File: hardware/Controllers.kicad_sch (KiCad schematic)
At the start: 1 part

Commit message: NEW SCHEMATIC
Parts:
- removed D7: D_TVS, symbol Device:D_TVS
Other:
- removed sheet IC_4
- added sheet IC_0 (ic_0.kicad_sch)
- sheet IC_1: file IC.kicad_sch -> ic_1.kicad_sch
- sheet IC_1 ports: added FUSE_IS1, LHI1, NSS, OUT1_0, OUT1_1, OUT1_2, OUT1_3, SCK; removed CSN, IS, LHI, OUT0, OUT1, OUT2, OUT3, SCLK
- sheet IC_2: file IC.kicad_sch -> ic_2.kicad_sch
- sheet IC_2 ports: added FUSE_IS2, LHI2, NSS, OUT2_0, OUT2_1, OUT2_2, OUT2_3, SCK; removed CSN, IS, LHI, OUT0, OUT1, OUT2, OUT3, SCLK
- sheet IC_3: file IC.kicad_sch -> ic_3.kicad_sch
- sheet IC_3 ports: added FUSE_IS3, LHI3, NSS, OUT3_0, OUT3_1, OUT3_2, OUT3_3, SCK; removed CSN, IS, LHI, OUT0, OUT1, OUT2, OUT3, SCLK
- note removed: "clk"
- note removed: "nss"
- note removed: "tvs na schemacie z konektorem"
- company: (none) -> Authors: Grzegorz Potocki Jędrzej Kasprzyk
- title: (none) -> PDUv3

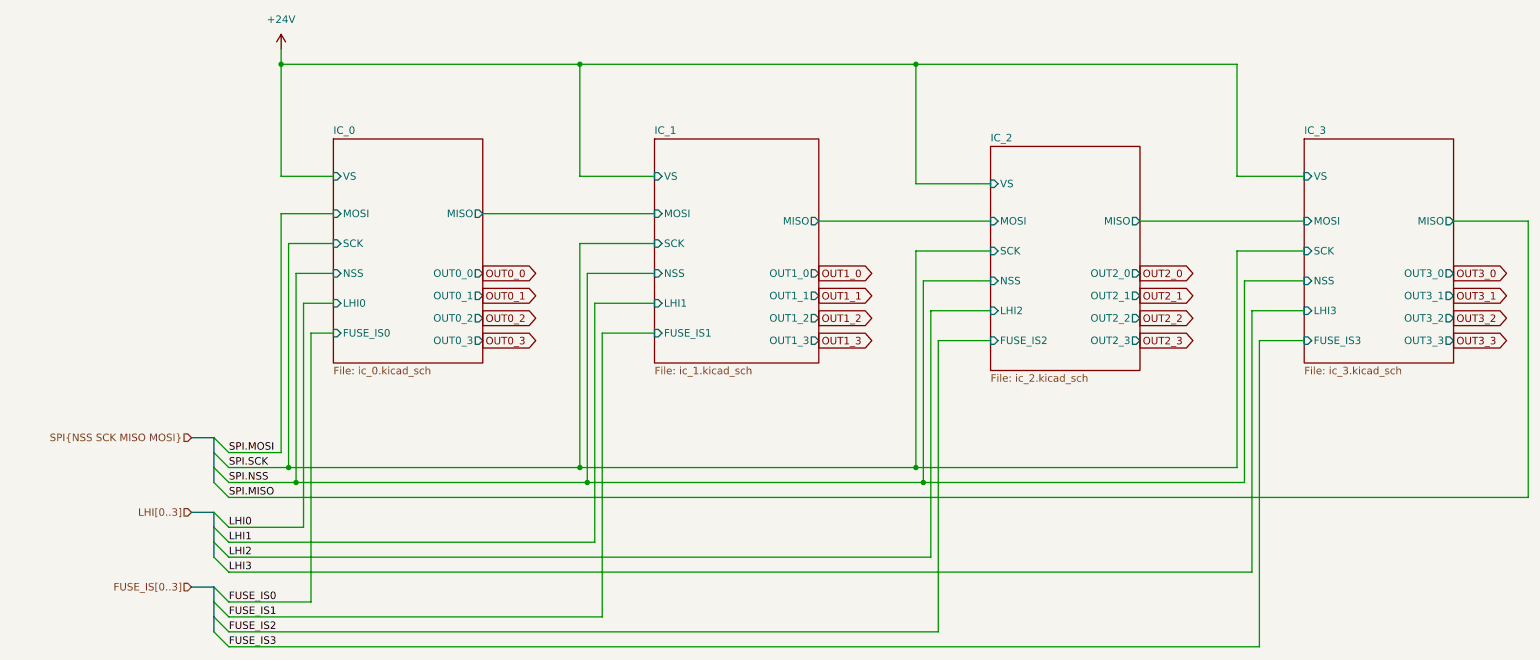
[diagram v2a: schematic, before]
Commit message: new pcb layout & can coppied from steeringwheel
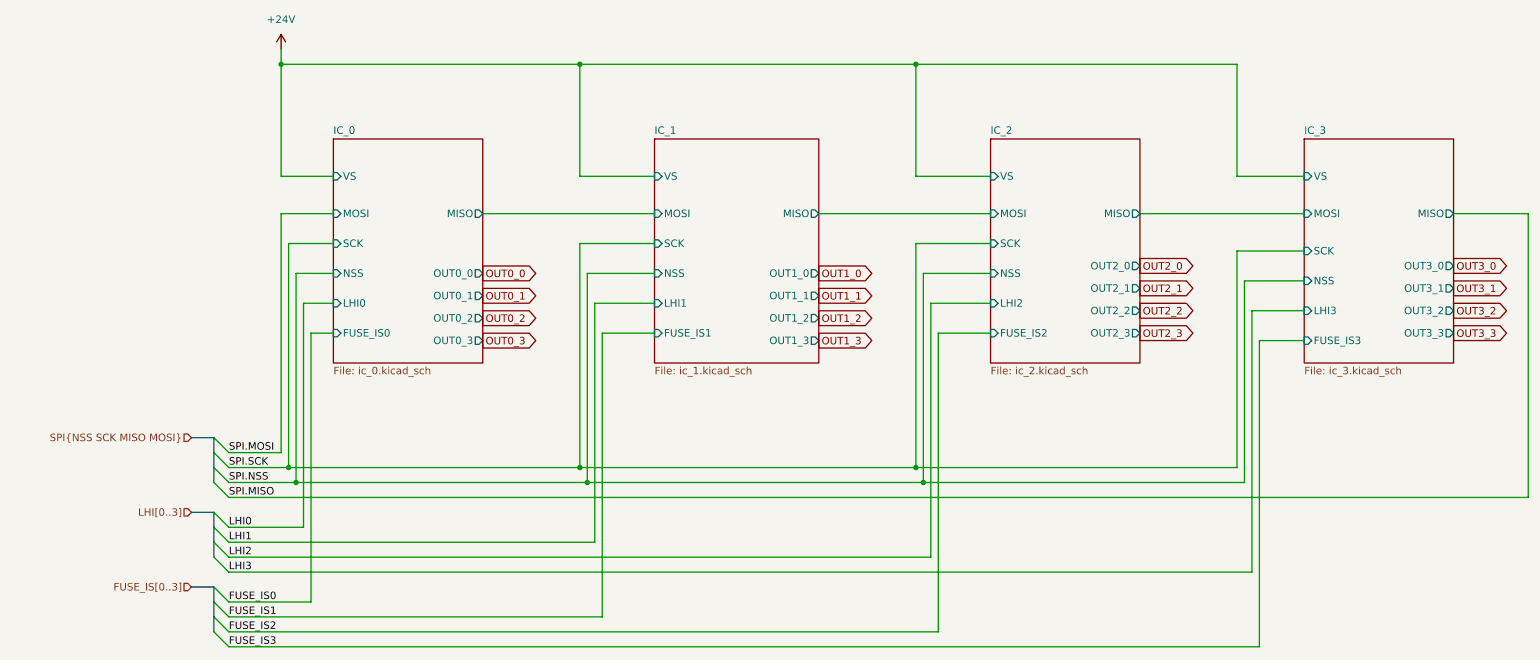
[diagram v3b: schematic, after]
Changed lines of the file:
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@@
 	(wire
 		(pts
-			(xy 171.45 134.62) (xy 171.45 92.71)
+			(xy 171.45 134.62) (xy 171.45 91.44)
 		)
 		(stroke
@@
 	(wire
 		(pts
-			(xy 170.18 87.63) (xy 181.61 87.63)
+			(xy 170.18 86.36) (xy 181.61 86.36)
 		)
 		(stroke
@@
 	(wire
 		(pts
-			(xy 273.05 77.47) (xy 260.35 77.47)
+			(xy 273.05 76.2) (xy 260.35 76.2)
 		)
 		(stroke
@@
 	(wire
 		(pts
-			(xy 181.61 97.79) (xy 172.72 97.79)
-		)
-		(stroke
-			(width 0)
-			(type default)
-		)
-	)
-	(wire
-		(pts
-			(xy 207.01 77.47) (xy 234.95 77.47)
+			(xy 181.61 96.52) (xy 172.72 96.52)
+		)
+		(stroke
+			(width 0)
+			(type default)
+		)
+	)
+	(wire
+		(pts
+			(xy 207.01 76.2) (xy 234.95 76.2)
 		)
 		(stroke
@@
 	(wire
 		(pts
-			(xy 273.05 124.46) (xy 273.05 77.47)
+			(xy 273.05 124.46) (xy 273.05 76.2)
 		)
 		(stroke
@@
 	(wire
 		(pts
-			(xy 168.91 71.12) (xy 181.61 71.12)
+			(xy 168.91 69.85) (xy 181.61 69.85)
 		)
 		(stroke
@@
 	(wire
 		(pts
+			(xy 152.4 76.2) (xy 181.61 76.2)
+		)
+		(stroke
+			(width 0)
+			(type default)
+		)
+	)
+	(wire
+		(pts
 			(xy 111.76 119.38) (xy 111.76 81.28)
 		)
@@
 	(wire
 		(pts
-			(xy 170.18 121.92) (xy 170.18 87.63)
+			(xy 170.18 121.92) (xy 170.18 86.36)
 		)
 		(stroke
@@
 	(wire
 		(pts
-			(xy 171.45 92.71) (xy 181.61 92.71)
-		)
-		(stroke
-			(width 0)
-			(type default)
-		)
-	)
-	(wire
-		(pts
-			(xy 168.91 50.8) (xy 168.91 71.12)
+			(xy 171.45 91.44) (xy 181.61 91.44)
+		)
+		(stroke
+			(width 0)
+			(type default)
+		)
+	)
+	(wire
+		(pts
+			(xy 168.91 50.8) (xy 168.91 69.85)
 		)
 		(stroke
@@
 	(wire
 		(pts
-			(xy 168.91 119.38) (xy 168.91 82.55)
+			(xy 168.91 119.38) (xy 168.91 81.28)
 		)
 		(stroke
@@
 	(wire
 		(pts
-			(xy 168.91 82.55) (xy 181.61 82.55)
+			(xy 168.91 81.28) (xy 181.61 81.28)
 		)
 		(stroke
@@
 	(wire
 		(pts
-			(xy 152.4 77.47) (xy 181.61 77.47)
-		)
-		(stroke
-			(width 0)
-			(type default)
-		)
-	)
-	(wire
-		(pts
 			(xy 60.96 50.8) (xy 111.76 50.8)
 		)
@@
 	(wire
 		(pts
-			(xy 172.72 97.79) (xy 172.72 147.32)
+			(xy 172.72 96.52) (xy 172.72 147.32)
 		)
 		(stroke
@@
 	(global_label "OUT2_3"
 		(shape output)
-		(at 207.01 97.79 0)
+		(at 207.01 96.52 0)
 		(fields_autoplaced yes)
 		(effects
@@
 		)
 		(property "Intersheetrefs" "${INTERSHEET_REFS}"
-			(at 217.0104 97.79 0)
+			(at 217.0104 96.52 0)
 			(effects
 				(font
@@
 	(global_label "OUT3_1"
 		(shape output)
-		(at 260.35 90.17 0)
+		(at 260.35 88.9 0)
 		(fields_autoplaced yes)
 		(effects
@@
 		)
 		(property "Intersheetrefs" "${INTERSHEET_REFS}"
-			(at 270.3504 90.17 0)
+			(at 270.3504 88.9 0)
 			(effects
 				(font
@@
 	(global_label "OUT2_1"
 		(shape output)
-		(at 207.01 90.17 0)
+		(at 207.01 88.9 0)
 		(fields_autoplaced yes)
 		(effects
@@
 		)
 		(property "Intersheetrefs" "${INTERSHEET_REFS}"
-			(at 217.0104 90.17 0)
+			(at 217.0104 88.9 0)
 			(effects
 				(font
@@
 	(global_label "OUT3_3"
 		(shape output)
-		(at 260.35 97.79 0)
+		(at 260.35 96.52 0)
 		(fields_autoplaced yes)
 		(effects
@@
 		)
 		(property "Intersheetrefs" "${INTERSHEET_REFS}"
-			(at 270.3504 97.79 0)
+			(at 270.3504 96.52 0)
 			(effects
 				(font
@@
 	(global_label "OUT2_0"
 		(shape output)
-		(at 207.01 86.36 0)
+		(at 207.01 85.09 0)
 		(fields_autoplaced yes)
 		(effects
@@
 		)
 		(property "Intersheetrefs" "${INTERSHEET_REFS}"
-			(at 217.0104 86.36 0)
+			(at 217.0104 85.09 0)
 			(effects
 				(font
@@
 	(global_label "OUT2_2"
 		(shape output)
-		(at 207.01 93.98 0)
+		(at 207.01 92.71 0)
 		(fields_autoplaced yes)
 		(effects
@@
 		)
 		(property "Intersheetrefs" "${INTERSHEET_REFS}"
-			(at 217.0104 93.98 0)
+			(at 217.0104 92.71 0)
 			(effects
 				(font
@@
 	(global_label "OUT3_2"
 		(shape output)
-		(at 260.35 93.98 0)
+		(at 260.35 92.71 0)
 		(fields_autoplaced yes)
 		(effects
@@
 		)
 		(property "Intersheetrefs" "${INTERSHEET_REFS}"
-			(at 270.3504 93.98 0)
+			(at 270.3504 92.71 0)
 			(effects
 				(font
@@
 	(global_label "OUT3_0"
 		(shape output)
-		(at 260.35 86.36 0)
+		(at 260.35 85.09 0)
 		(fields_autoplaced yes)
 		(effects
@@
 		)
 		(property "Intersheetrefs" "${INTERSHEET_REFS}"
-			(at 270.3504 86.36 0)
+			(at 270.3504 85.09 0)
 			(effects
 				(font
@@
 		(dnp no)
 		(fields_autoplaced yes)
-		(property "Reference" "#PWR030"
+		(property "Reference" "#PWR028"
 			(at 60.96 52.07 0)
 			(effects
@@
 		)
 		(instances
-			(project ""
+			(project "PUTM_EV_PDMv2_2024"
 				(path "/b652b05a-4e3d-4ad1-b032-18886abe7d45/fd7d6fe4-610a-44c2-815e-0a8f21ae1980"
-					(reference "#PWR030")
+					(reference "#PWR028")
 					(unit 1)
 				)
@@
 		)
 		(pin "MISO" output
-			(at 152.4 77.47 0)
+			(at 152.4 76.2 0)
 			(effects
 				(font
@@
 	)
 	(sheet
-		(at 181.61 64.77)
+		(at 181.61 63.5)
 		(size 25.4 38.1)
 		(exclude_from_sim no)
@@
 		)
 		(property "Sheetname" "IC_2"
-			(at 181.61 64.0584 0)
+			(at 181.61 62.7884 0)
 			(effects
 				(font
@@
 		)
 		(property "Sheetfile" "ic_2.kicad_sch"
-			(at 181.61 103.4546 0)
+			(at 181.61 102.1846 0)
 			(effects
 				(font
@@
 		)
 		(pin "VS" input
-			(at 181.61 71.12 180)
+			(at 181.61 69.85 180)
 			(effects
 				(font
@@
 		)
 		(pin "MOSI" input
-			(at 181.61 77.47 180)
+			(at 181.61 76.2 180)
 			(effects
 				(font
@@
 		)
 		(pin "LHI2" input
-			(at 181.61 92.71 180)
+			(at 181.61 91.44 180)
 			(effects
 				(font
@@
 		)
 		(pin "MISO" output
-			(at 207.01 77.47 0)
+			(at 207.01 76.2 0)
 			(effects
 				(font
@@
 		)
 		(pin "NSS" input
-			(at 181.61 87.63 180)
+			(at 181.61 86.36 180)
 			(effects
 				(font
@@
 		)
 		(pin "FUSE_IS2" input
-			(at 181.61 97.79 180)
+			(at 181.61 96.52 180)
 			(effects
 				(font
@@
 		)
 		(pin "SCK" input
-			(at 181.61 82.55 180)
+			(at 181.61 81.28 180)
 			(effects
 				(font
@@
 		)
 		(pin "OUT2_1" output
-			(at 207.01 90.17 0)
+			(at 207.01 88.9 0)
 			(effects
 				(font
@@
 		)
 		(pin "OUT2_3" output
-			(at 207.01 97.79 0)
+			(at 207.01 96.52 0)
 			(effects
 				(font
@@
 		)
 		(pin "OUT2_2" output
-			(at 207.01 93.98 0)
+			(at 207.01 92.71 0)
 			(effects
 				(font
@@
 		)
 		(pin "OUT2_0" output
-			(at 207.01 86.36 0)
+			(at 207.01 85.09 0)
 			(effects
 				(font
@@
 		)
 		(pin "MISO" output
-			(at 260.35 77.47 0)
+			(at 260.35 76.2 0)
 			(effects
 				(font
@@
 		)
 		(pin "MOSI" input
-			(at 234.95 77.47 180)
+			(at 234.95 76.2 180)
 			(effects
 				(font
@@
 		)
 		(pin "OUT3_3" output
-			(at 260.35 97.79 0)
+			(at 260.35 96.52 0)
 			(effects
 				(font
@@
 		)
 		(pin "OUT3_2" output
-			(at 260.35 93.98 0)
+			(at 260.35 92.71 0)
 			(effects
 				(font
@@
 		)
 		(pin "OUT3_0" output
-			(at 260.35 86.36 0)
+			(at 260.35 85.09 0)
 			(effects
 				(font
@@
 		)
 		(pin "OUT3_1" output
-			(at 260.35 90.17 0)
-			(effects
-				(font
+			(at 260.35 88.9 0)
+			(effects
+				(font

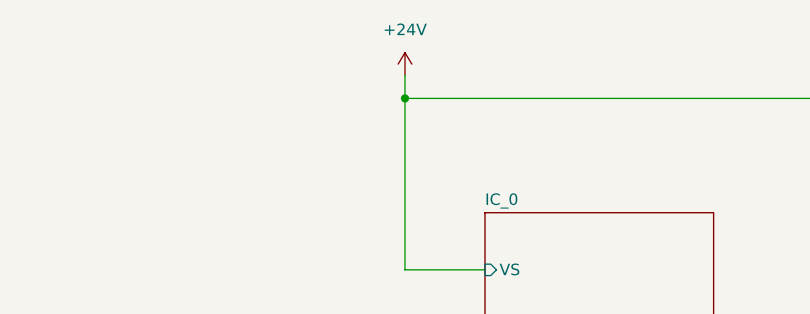
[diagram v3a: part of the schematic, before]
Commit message: pcb layout - controlers power->battery, added mounting holes
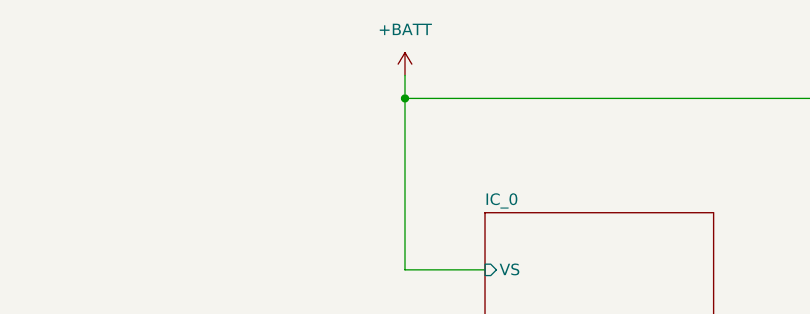
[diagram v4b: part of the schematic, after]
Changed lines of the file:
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@@
 	)
 	(symbol
-		(lib_id "power:+24V")
+		(lib_id "power:+BATT")
 		(at 60.96 48.26 0)
 		(unit 1)
@@
 		(dnp no)
 		(fields_autoplaced yes)
-		(property "Reference" "#PWR028"
+		(property "Reference" "#PWR011"
 			(at 60.96 52.07 0)
 			(effects
@@
 			)
 		)
-		(property "Value" "+24V"
+		(property "Value" "+BATT"
 			(at 60.96 43.18 0)
 			(effects
@@
 			)
 		)
-		(property "Description" "Power symbol creates a global label with name \"+24V\""
+		(property "Description" "Power symbol creates a global label with name \"+BATT\""
 			(at 60.96 48.26 0)
 			(effects
@@
 			(project "PUTM_EV_PDMv2_2024"
 				(path "/b652b05a-4e3d-4ad1-b032-18886abe7d45/fd7d6fe4-610a-44c2-815e-0a8f21ae1980"
-					(reference "#PWR028")
+					(reference "#PWR011")
 					(unit 1)
 				)
